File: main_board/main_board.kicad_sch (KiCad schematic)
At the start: 107 parts, among them J1 Conn_01x08_S8B-PH-K-S(LF)(SN), J2 Conn_02x20_2214SM-40G-75-PCR, J3 Conn_01x02_B2B-PH-K-S(LF)(SN), J4 USB_C_USB4930-00-A, J5 Conn_01x03_MC34747, J6 Conn_01x04_FFC3B11-04-T, Q1 Q_BC817-25, Q3 Q_BC817-25, SW1 SW_B3FS-1050, SW2 SW_B3FS-1050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

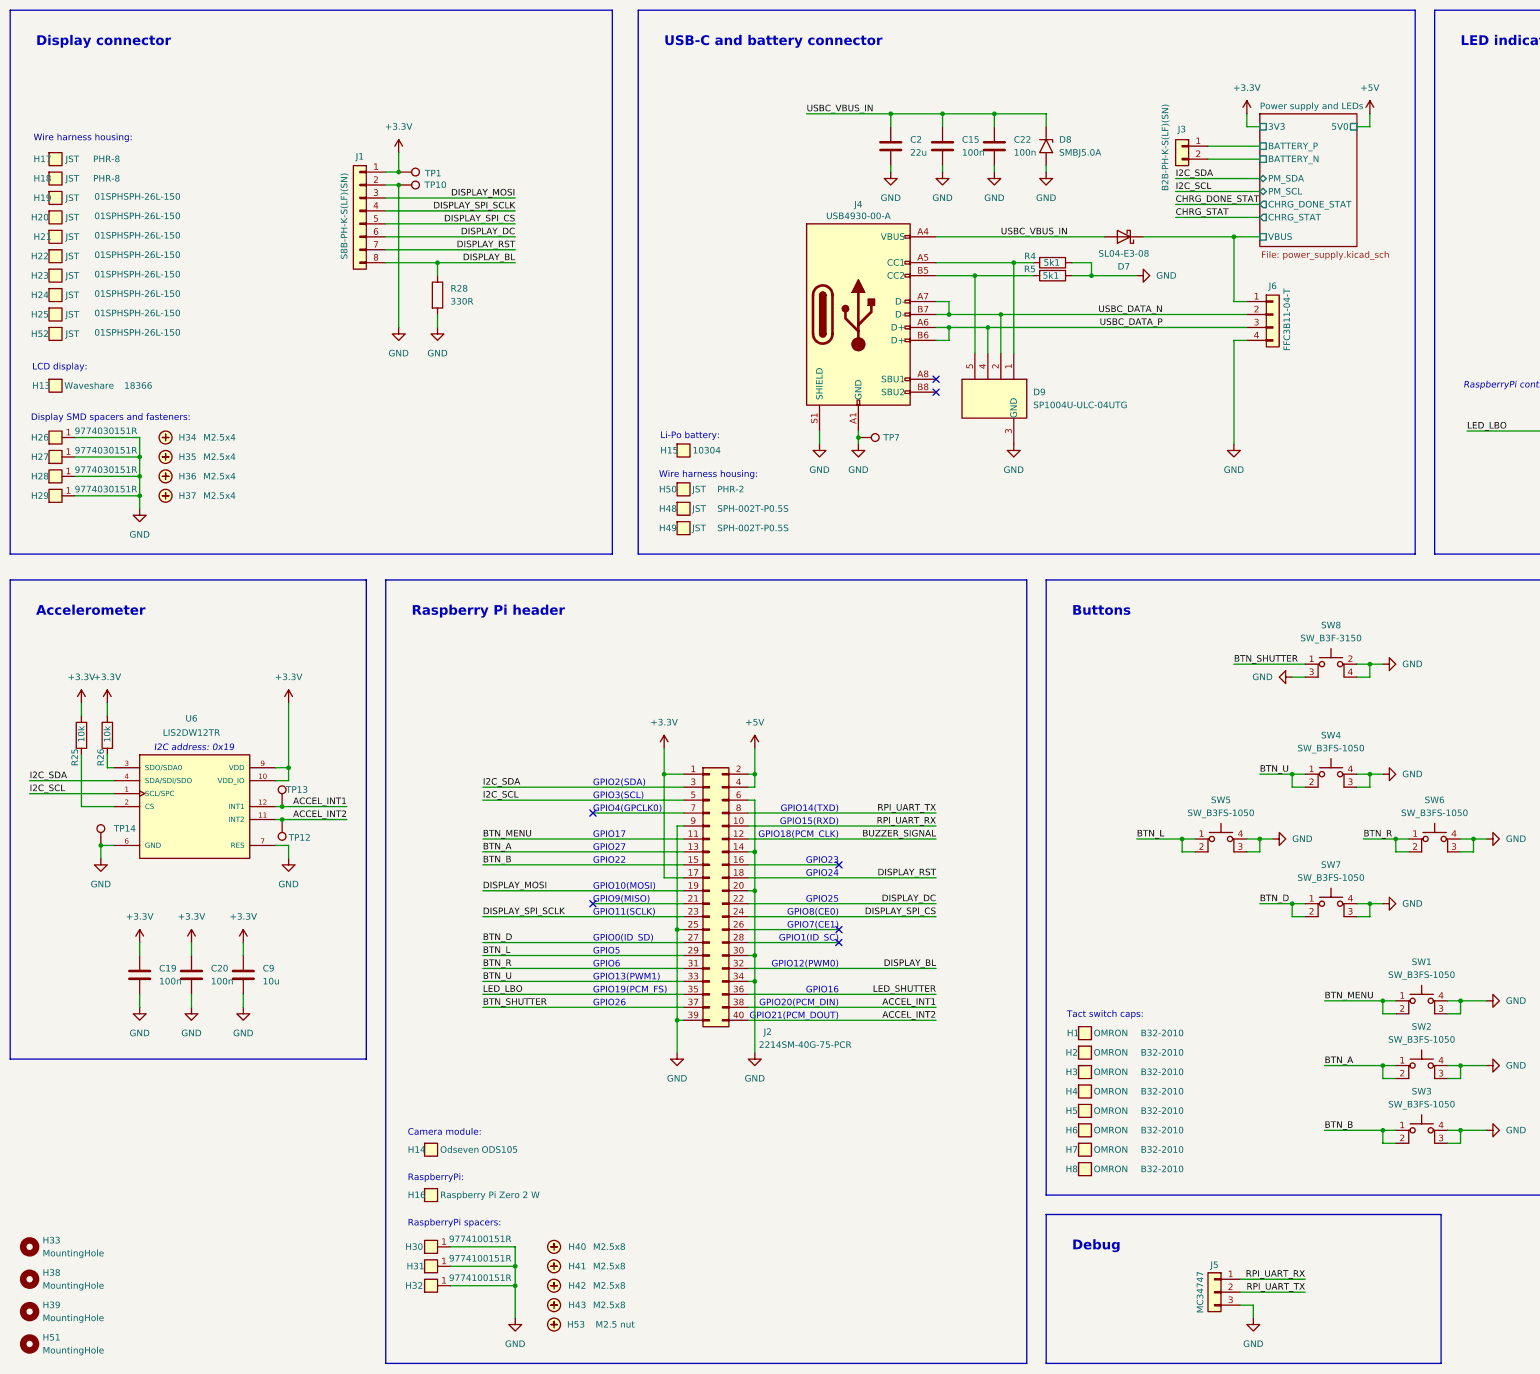
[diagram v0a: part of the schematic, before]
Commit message: Add TODOs from rev.1.1 bringup
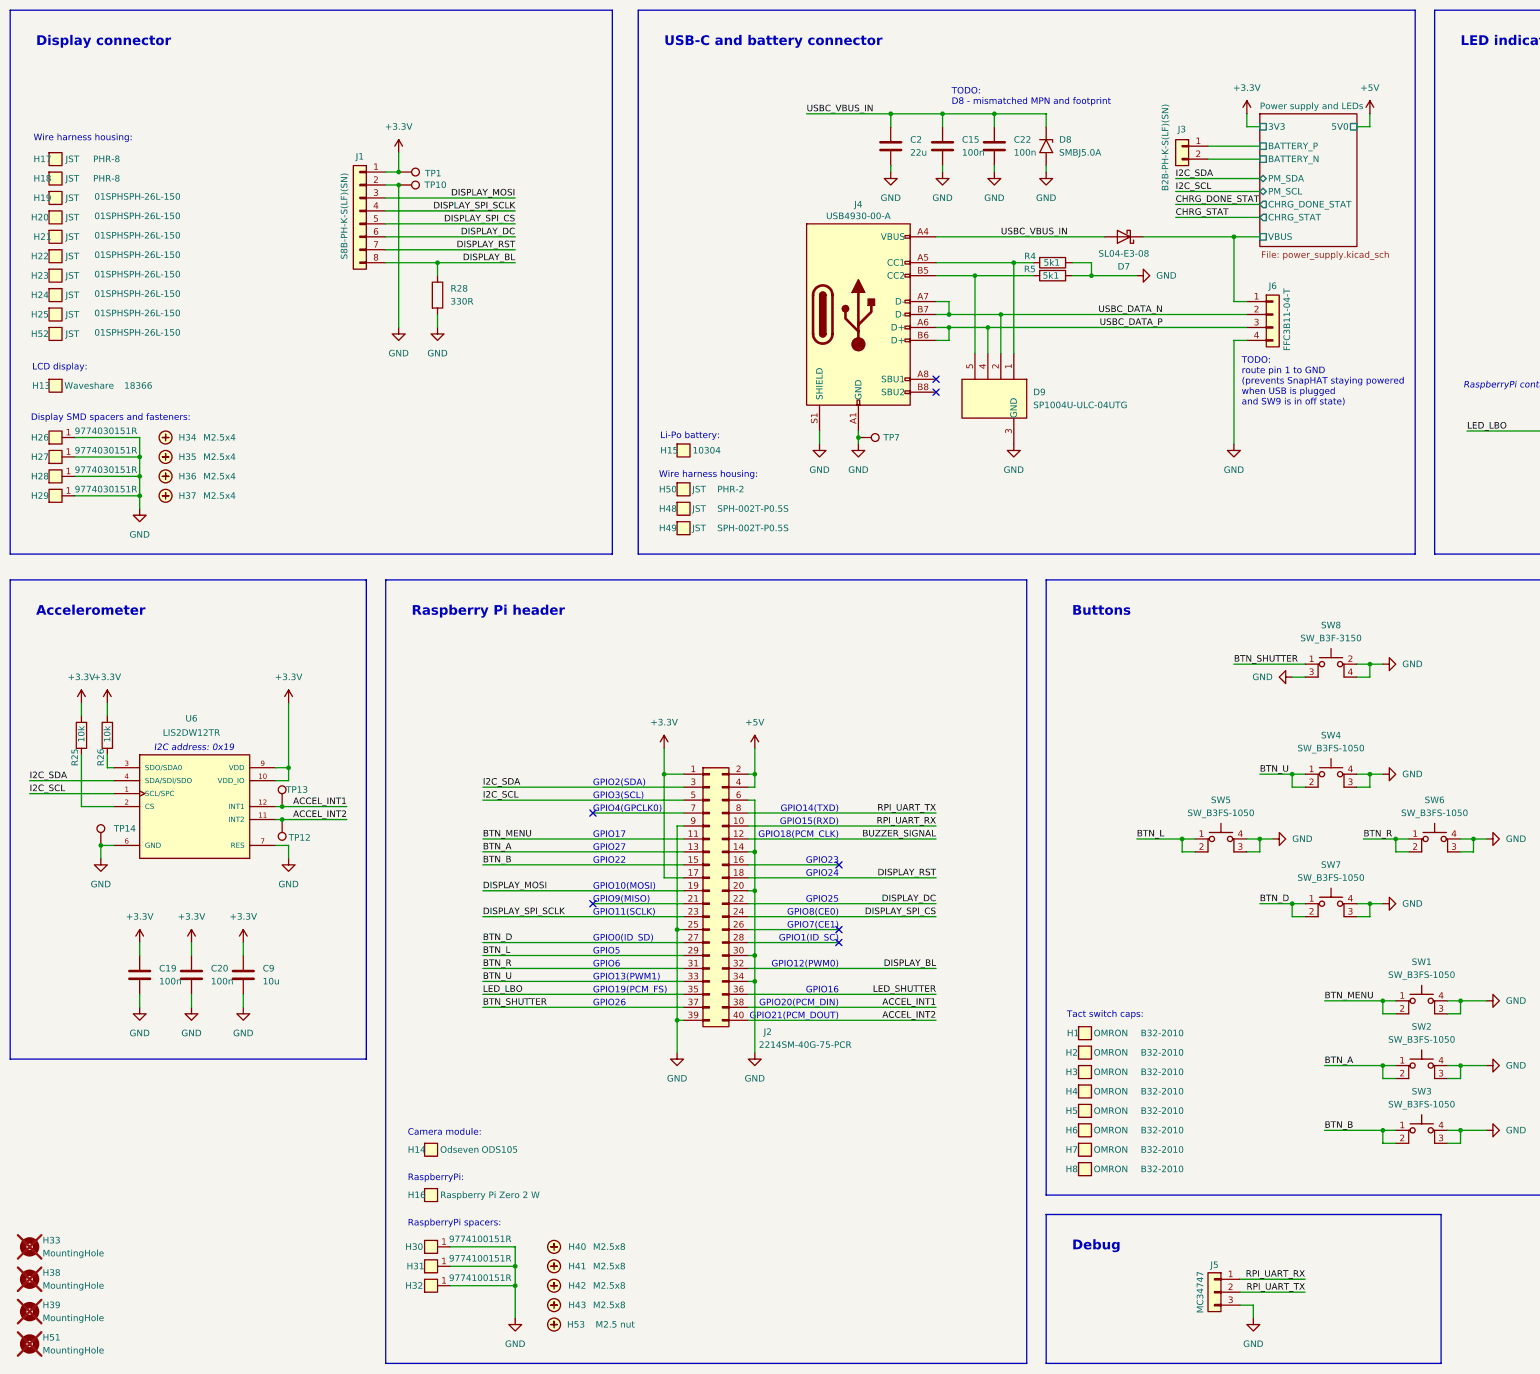
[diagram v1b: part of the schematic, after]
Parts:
- H33, H38, H39, H51: now not fitted
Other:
- note added: "TODO: D8 - mismatched MPN and footprint"
- note added: "TODO: route pin 1 to GND (prevents SnapHAT staying powered when USB is plugged and SW9 is in off state)"

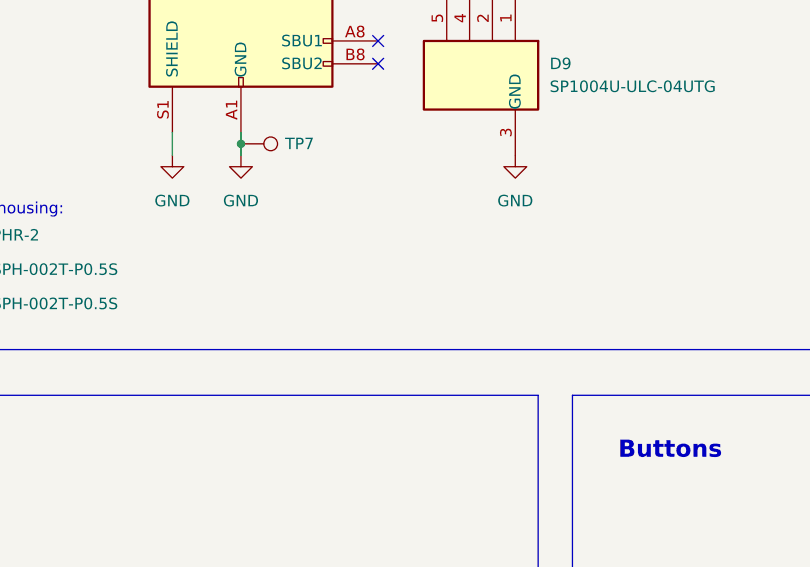
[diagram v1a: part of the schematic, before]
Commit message: Update README (real life photos, wire harness info), add a TODO
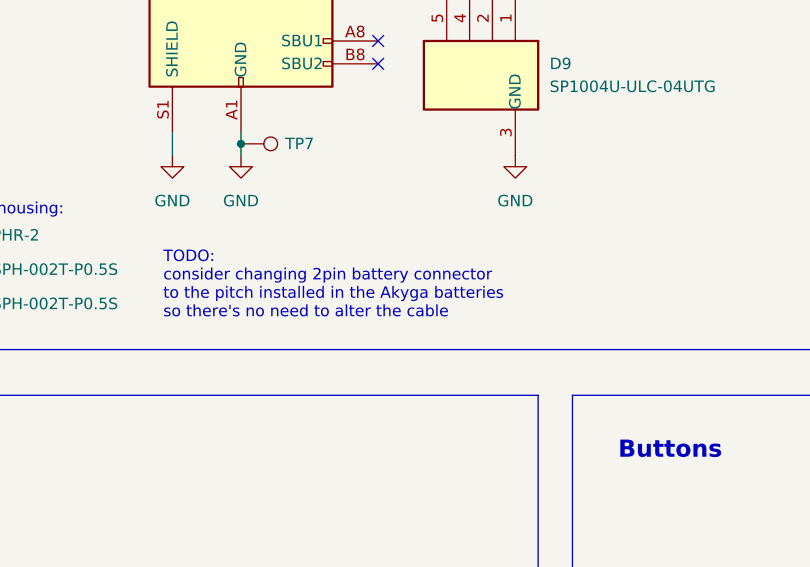
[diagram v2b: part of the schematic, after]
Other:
- note added: "TODO: consider changing 2pin battery connector to the pitch installed in the Akyga batteries so there's no need to alter the cable"
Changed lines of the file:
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@@
+		)
+	)
+	(text "TODO:\nconsider changing 2pin battery connector\nto the pitch installed in the Akyga batteries\nso there's no need to alter the cable"
+		(exclude_from_sim no)
+		(at 172.974 116.078 0)
+		(effects
+			(font
+				(face "Quicksand")
+				(size 1.27 1.27)
+			)
+			(justify left)
 		)
 	)
